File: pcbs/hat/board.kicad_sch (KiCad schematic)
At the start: 1 part, among them U17 NUCLEO-F401RE

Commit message: wip
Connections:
- net MEM_MISO: now also U17.CN7_2 (PC11); no longer U17.CN7_35 (PC2)
- net MEM_MOSI: now also U17.CN7_3 (PC12); no longer U17.CN7_37 (PC3)
- net MEM_SCK: now also U17.CN7_1 (PC10); no longer U17.CN10_25 (PB10)
- net SENSOR_13: now also U17.CN10_2 (PC8); no longer U17.CN10_4 (PC6)
- net SENSOR_23: now also U17.CN10_6 (PC5); no longer U17.CN10_19 (PC7)
- net SENSOR_33: no longer U17.CN10_2 (PC8)
- net SENSOR_43: no longer U17.CN10_1 (PC9)
- net SENSOR_53: no longer U17.CN10_16 (PB12)
- net SENSOR_63: no longer U17.CN10_30 (PB13)
- net SENSOR_73: no longer U17.CN10_28 (PB14)
- net SENSOR_83: no longer U17.CN10_26 (PB15)
- net SIGNAL_10: now also U17.CN10_12 (PA12); no longer U17.CN7_21 (PB7)
- net SIGNAL_11: now also U17.CN10_4 (PC6); no longer U17.CN10_13 (PA6)
- net SIGNAL_20: now also U17.CN10_16 (PB12); no longer U17.CN10_27 (PB4)
- net SIGNAL_21: now also U17.CN10_14 (PA11); no longer U17.CN10_15 (PA7)
- net SIGNAL_30: no longer U17.CN10_17 (PB6)
- net SIGNAL_31: no longer U17.CN7_34 (PB0)
- net SIGNAL_40: no longer U17.CN10_29 (PB5)
- net SIGNAL_41: no longer U17.CN10_24 (PB1)
- net SIGNAL_50: no longer U17.CN7_2 (PC11)
- net SIGNAL_51: no longer U17.CN10_23 (PA8)
- net SIGNAL_60: no longer U17.CN7_1 (PC10)
- net SIGNAL_61: no longer U17.CN10_21 (PA9)
- net SIGNAL_70: no longer U17.CN7_3 (PC12)
- net SIGNAL_71: no longer U17.CN10_33 (PA10)
- net SIGNAL_80: no longer U17.CN7_17 (PA15)
- net SIGNAL_81: no longer U17.CN10_14 (PA11)
- net ~{MEM_CE}: now also U17.CN7_4 (PD2); no longer U17.CN7_36 (PC1/PB9)

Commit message: wip
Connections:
- net SENSOR_13: now also U17.CN10_4 (PC6); no longer U17.CN10_2 (PC8)
- net SENSOR_33: now also U17.CN10_34 (PC4)
- net SENSOR_43: now also U17.CN10_29 (PB5)
- net SIGNAL_11: now also U17.CN10_2 (PC8); no longer U17.CN10_4 (PC6)
- net SIGNAL_21: now also U17.CN10_24 (PB1); no longer U17.CN10_14 (PA11)
- net SIGNAL_30: now also U17.CN10_30 (PB13)
- net SIGNAL_31: now also U17.CN10_33 (PA10)
- net SIGNAL_40: now also U17.CN10_28 (PB14)
- net SIGNAL_41: now also U17.CN10_27 (PB4)
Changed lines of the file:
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@@
+    (stroke (width 0) (type default) (color 0 0 0 0))
+  )
+  (bus_entry (at 170.18 57.15) (size -2.54 -2.54)
     (stroke (width 0) (type default) (color 0 0 0 0))
   )
@@
     (stroke (width 0) (type default) (color 0 0 0 0))
   )
-  (bus_entry (at 101.6 77.47) (size 2.54 -2.54)
+  (bus_entry (at 101.6 85.09) (size 2.54 -2.54)
     (stroke (width 0) (type default) (color 0 0 0 0))
   )
@@
     (stroke (width 0) (type default) (color 0 0 0 0))
   )
+  (bus_entry (at 101.6 95.25) (size 2.54 -2.54)
+    (stroke (width 0) (type default) (color 0 0 0 0))
+  )
+  (bus_entry (at 107.95 30.48) (size 2.54 -2.54)
+    (stroke (width 0) (type default) (color 0 0 0 0))
+  )
   (bus_entry (at -71.755 120.65) (size 2.54 -2.54)
     (stroke (width 0) (type default) (color 0 0 0 0))
@@
     (stroke (width 0) (type default) (color 0 0 0 0))
   )
+  (bus_entry (at 101.6 92.71) (size 2.54 -2.54)
+    (stroke (width 0) (type default) (color 0 0 0 0))
+  )
+  (bus_entry (at 101.6 74.93) (size 2.54 -2.54)
+    (stroke (width 0) (type default) (color 0 0 0 0))
+  )
   (bus_entry (at -68.58 90.17) (size 2.54 -2.54)
     (stroke (width 0) (type default) (color 0 0 0 0))
   )
+  (bus_entry (at 101.6 113.03) (size 2.54 -2.54)
+    (stroke (width 0) (type default) (color 0 0 0 0))
+  )
+  (bus_entry (at 101.6 110.49) (size 2.54 -2.54)
+    (stroke (width 0) (type default) (color 0 0 0 0))
+  )
   (bus_entry (at 101.6 107.95) (size 2.54 -2.54)
     (stroke (width 0) (type default) (color 0 0 0 0))
@@
     (stroke (width 0) (type default) (color 0 0 0 0))
   )
+  (bus_entry (at 163.83 30.48) (size -2.54 -2.54)
+    (stroke (width 0) (type default) (color 0 0 0 0))
+  )
   (bus_entry (at -68.58 107.95) (size 2.54 -2.54)
     (stroke (width 0) (type default) (color 0 0 0 0))
@@
     (stroke (width 0) (type default) (color 0 0 0 0))
   )
+  (wire (pts (xy 104.14 110.49) (xy 120.65 110.49))
+    (stroke (width 0) (type default) (color 0 0 0 0))
+  )
   (bus (pts (xy 98.425 19.05) (xy 170.18 19.05))
     (stroke (width 0) (type default) (color 0 0 0 0))
@@
     (stroke (width 0) (type default) (color 0 0 0 0))
   )
-  (bus (pts (xy 101.6 77.47) (xy 101.6 80.01))
-    (stroke (width 0) (type default) (color 0 0 0 0))
-  )
-  (bus (pts (xy 101.6 80.01) (xy 101.6 107.95))
-    (stroke (width 0) (type default) (color 0 0 0 0))
-  )
-  (bus (pts (xy 101.6 107.95) (xy 101.6 146.05))
+  (bus (pts (xy 101.6 80.01) (xy 101.6 85.09))
+    (stroke (width 0) (type default) (color 0 0 0 0))
+  )
+  (bus (pts (xy 101.6 107.95) (xy 101.6 110.49))
+    (stroke (width 0) (type default) (color 0 0 0 0))
+  )
+  (bus (pts (xy 101.6 110.49) (xy 101.6 113.03))
+    (stroke (width 0) (type default) (color 0 0 0 0))
+  )
+  (bus (pts (xy 101.6 74.93) (xy 101.6 80.01))
+    (stroke (width 0) (type default) (color 0 0 0 0))
+  )
+  (bus (pts (xy 170.18 57.15) (xy 170.18 59.69))
     (stroke (width 0) (type default) (color 0 0 0 0))
   )
@@
     (stroke (width 0) (type default) (color 0 0 0 0))
   )
-  (wire (pts (xy 104.14 74.93) (xy 120.65 74.93))
+  (bus (pts (xy 101.6 95.25) (xy 101.6 107.95))
+    (stroke (width 0) (type default) (color 0 0 0 0))
+  )
+  (wire (pts (xy 104.14 82.55) (xy 120.65 82.55))
     (stroke (width 0) (type default) (color 0 0 0 0))
   )
@@
     (stroke (width 0) (type default) (color 0 0 0 0))
   )
+  (wire (pts (xy 167.64 54.61) (xy 151.13 54.61))
+    (stroke (width 0) (type default) (color 0 0 0 0))
+  )
   (bus (pts (xy 31.75 19.05) (xy 98.425 19.05))
     (stroke (width 0) (type default) (color 0 0 0 0))
@@
     (stroke (width 0) (type default) (color 0 0 0 0))
   )
+  (wire (pts (xy 104.14 107.95) (xy 120.65 107.95))
+    (stroke (width 0) (type default) (color 0 0 0 0))
+  )
   (wire (pts (xy -28.575 110.49) (xy -12.065 110.49))
     (stroke (width 0) (type default) (color 0 0 0 0))
@@
     (stroke (width 0) (type default) (color 0 0 0 0))
   )
+  (wire (pts (xy 104.14 90.17) (xy 120.65 90.17))
+    (stroke (width 0) (type default) (color 0 0 0 0))
+  )
   (wire (pts (xy 104.14 77.47) (xy 120.65 77.47))
     (stroke (width 0) (type default) (color 0 0 0 0))
   )
+  (wire (pts (xy 110.49 27.94) (xy 127 27.94))
+    (stroke (width 0) (type default) (color 0 0 0 0))
+  )
   (wire (pts (xy -28.575 105.41) (xy -12.065 105.41))
     (stroke (width 0) (type default) (color 0 0 0 0))
@@
     (stroke (width 0) (type default) (color 0 0 0 0))
   )
+  (bus (pts (xy 101.6 113.03) (xy 101.6 146.05))
+    (stroke (width 0) (type default) (color 0 0 0 0))
+  )
   (wire (pts (xy 81.28 67.31) (xy 80.01 67.31))
     (stroke (width 0) (type default) (color 0 0 0 0))
@@
     (stroke (width 0) (type default) (color 0 0 0 0))
   )
+  (wire (pts (xy 161.29 27.94) (xy 144.78 27.94))
+    (stroke (width 0) (type default) (color 0 0 0 0))
+  )
   (wire (pts (xy 167.64 57.15) (xy 151.13 57.15))
     (stroke (width 0) (type default) (color 0 0 0 0))
   )
+  (wire (pts (xy 104.14 92.71) (xy 120.65 92.71))
+    (stroke (width 0) (type default) (color 0 0 0 0))
+  )
   (bus (pts (xy 101.6 146.05) (xy 261.62 146.05))
     (stroke (width 0) (type default) (color 0 0 0 0))
@@
     (stroke (width 0) (type default) (color 0 0 0 0))
   )
+  (bus (pts (xy 101.6 85.09) (xy 101.6 92.71))
+    (stroke (width 0) (type default) (color 0 0 0 0))
+  )
   (wire (pts (xy -66.04 87.63) (xy -49.53 87.63))
     (stroke (width 0) (type default) (color 0 0 0 0))
@@
     (stroke (width 0) (type default) (color 0 0 0 0))
   )
-  (bus (pts (xy 101.6 44.45) (xy 101.6 77.47))
+  (bus (pts (xy 101.6 44.45) (xy 101.6 74.93))
+    (stroke (width 0) (type default) (color 0 0 0 0))
+  )
+  (wire (pts (xy 104.14 72.39) (xy 120.65 72.39))
     (stroke (width 0) (type default) (color 0 0 0 0))
   )
@@
     (stroke (width 0) (type default) (color 0 0 0 0))
   )
-  (bus (pts (xy 170.18 19.05) (xy 170.18 59.69))
+  (bus (pts (xy 170.18 19.05) (xy 170.18 57.15))
+    (stroke (width 0) (type default) (color 0 0 0 0))
+  )
+  (bus (pts (xy 101.6 92.71) (xy 101.6 95.25))
     (stroke (width 0) (type default) (color 0 0 0 0))
   )
@@
     (effects (font (size 1.27 1.27)) (justify left bottom))
   )
-  (label "SIGNAL_21" (at 105.41 74.93 0)
+  (label "SIGNAL_21" (at 105.41 82.55 0)
     (effects (font (size 1.27 1.27)) (justify left bottom))
   )
@@
     (effects (font (size 1.27 1.27)) (justify left bottom))
   )
-  (label "SIGNAL_41" (at -65.405 95.25 0)
-    (effects (font (size 1.27 1.27)) (justify left bottom))
-  )
-  (label "SIGNAL_30" (at -65.405 107.95 0)
-    (effects (font (size 1.27 1.27)) (justify left bottom))
-  )
-  (label "SENSOR_33" (at -107.95 97.155 180)
+  (label "SIGNAL_41" (at 106.68 90.17 0)
+    (effects (font (size 1.27 1.27)) (justify left bottom))
+  )
+  (label "SIGNAL_30" (at 106.045 107.95 0)
+    (effects (font (size 1.27 1.27)) (justify left bottom))
+  )
+  (label "SENSOR_33" (at 165.1 54.61 180)
     (effects (font (size 1.27 1.27)) (justify right bottom))
   )
@@
     (effects (font (size 1.27 1.27)) (justify left bottom))
   )
-  (label "SIGNAL_40" (at -65.405 105.41 0)
-    (effects (font (size 1.27 1.27)) (justify left bottom))
-  )
-  (label "SIGNAL_11" (at 166.37 59.69 180)
-    (effects (font (size 1.27 1.27)) (justify right bottom))
-  )
-  (label "SENSOR_43" (at -107.95 99.695 180)
+  (label "SIGNAL_40" (at 107.95 110.49 0)
+    (effects (font (size 1.27 1.27)) (justify left bottom))
+  )
+  (label "SIGNAL_11" (at 163.83 64.77 180)
+    (effects (font (size 1.27 1.27)) (justify right bottom))
+  )
+  (label "SENSOR_43" (at 115.57 92.71 180)
     (effects (font (size 1.27 1.27)) (justify right bottom))
   )
@@
     (effects (font (size 1.27 1.27)) (justify left bottom))
   )
-  (label "SIGNAL_31" (at -27.94 87.63 0)
+  (label "SIGNAL_31" (at 106.68 72.39 0)
     (effects (font (size 1.27 1.27)) (justify left bottom))
   )
@@
     (effects (font (size 1.27 1.27)) (justify left bottom))
   )
-  (label "SENSOR_13" (at 167.005 64.77 180)
-    (effects (font (size 1.27 1.27)) (justify right bottom))
-  )
+  (label "SENSOR_13" (at 164.465 59.69 180)
+    (effects (font (size 1.27 1.27)) (justify right bottom))
+  )

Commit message: finish the pin assignment
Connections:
- net GND: now also U17.CN10_20 (GND_S2), U17.CN10_9 (GND_S2), U17.CN5_7 (GND_S6), U17.CN6_6 (GND), U17.CN6_7 (GND)
- net SENSOR_13: now also U17.CN10_2 (PC8); no longer U17.CN10_4 (PC6)
- net SENSOR_53: now also U17.CN10_25 (PB10)
- net SENSOR_63: now also U17.CN10_21 (PA9)
- net SENSOR_73: now also U17.CN7_36 (PC1/PB9)
- net SENSOR_83: now also U17.CN7_37 (PC3)
- net SIGNAL_11: now also U17.CN10_4 (PC6); no longer U17.CN10_2 (PC8)
- net SIGNAL_30: now also U17.CN10_33 (PA10); no longer U17.CN10_30 (PB13)
- net SIGNAL_31: now also U17.CN10_30 (PB13); no longer U17.CN10_33 (PA10)
- net SIGNAL_50: now also U17.CN10_23 (PA8)
- net SIGNAL_51: now also U17.CN10_22 (PB2)
- net SIGNAL_60: now also U17.CN10_19 (PC7)
- net SIGNAL_61: now also U17.CN10_17 (PB6)
- net SIGNAL_70: now also U17.CN7_38 (PC0/PB8)
- net SIGNAL_71: now also U17.CN7_30 (PA1)
- net SIGNAL_80: now also U17.CN7_35 (PC2)
- net SIGNAL_81: now also U17.CN7_28 (PA0)

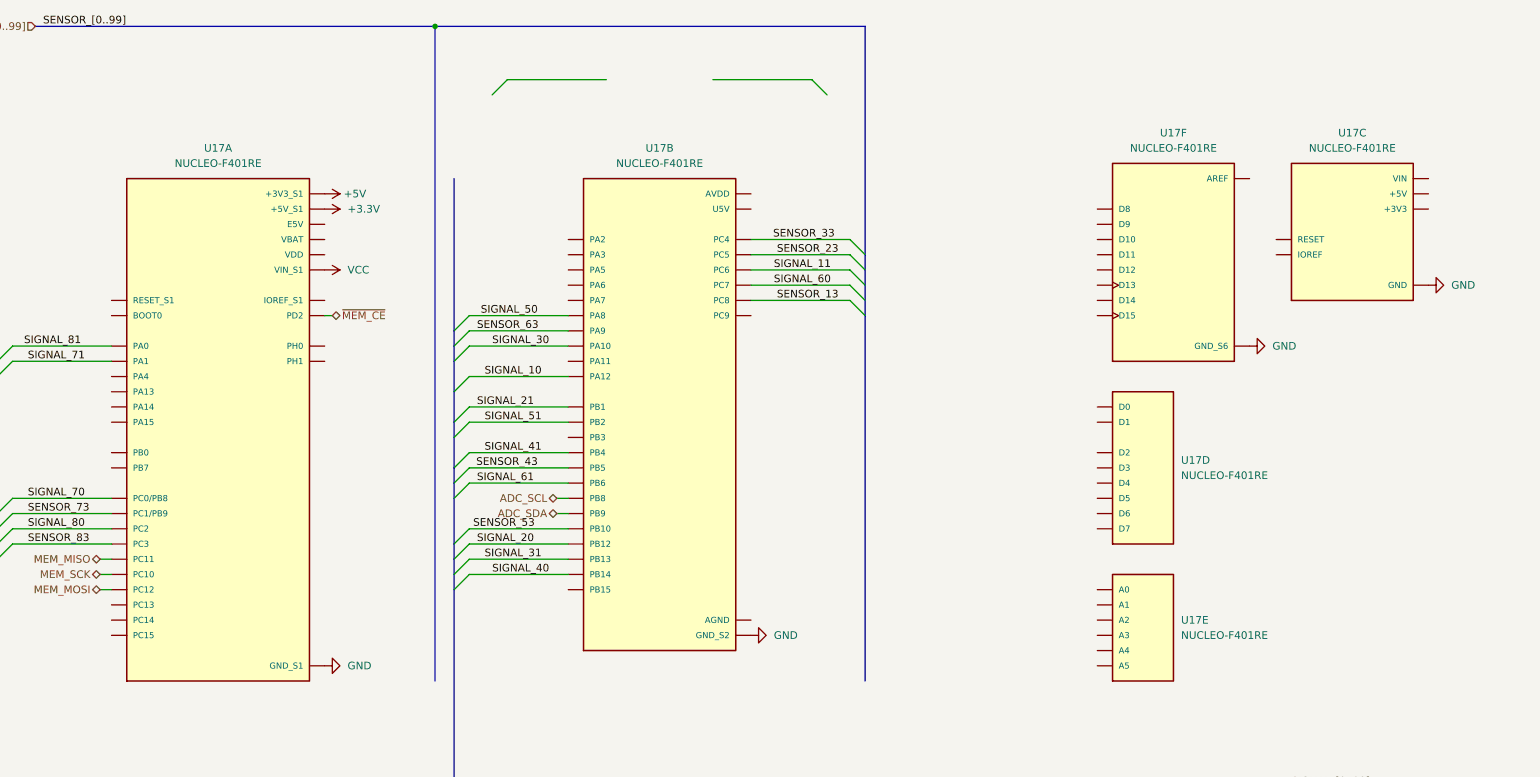
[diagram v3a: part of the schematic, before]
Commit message: reassign adc's
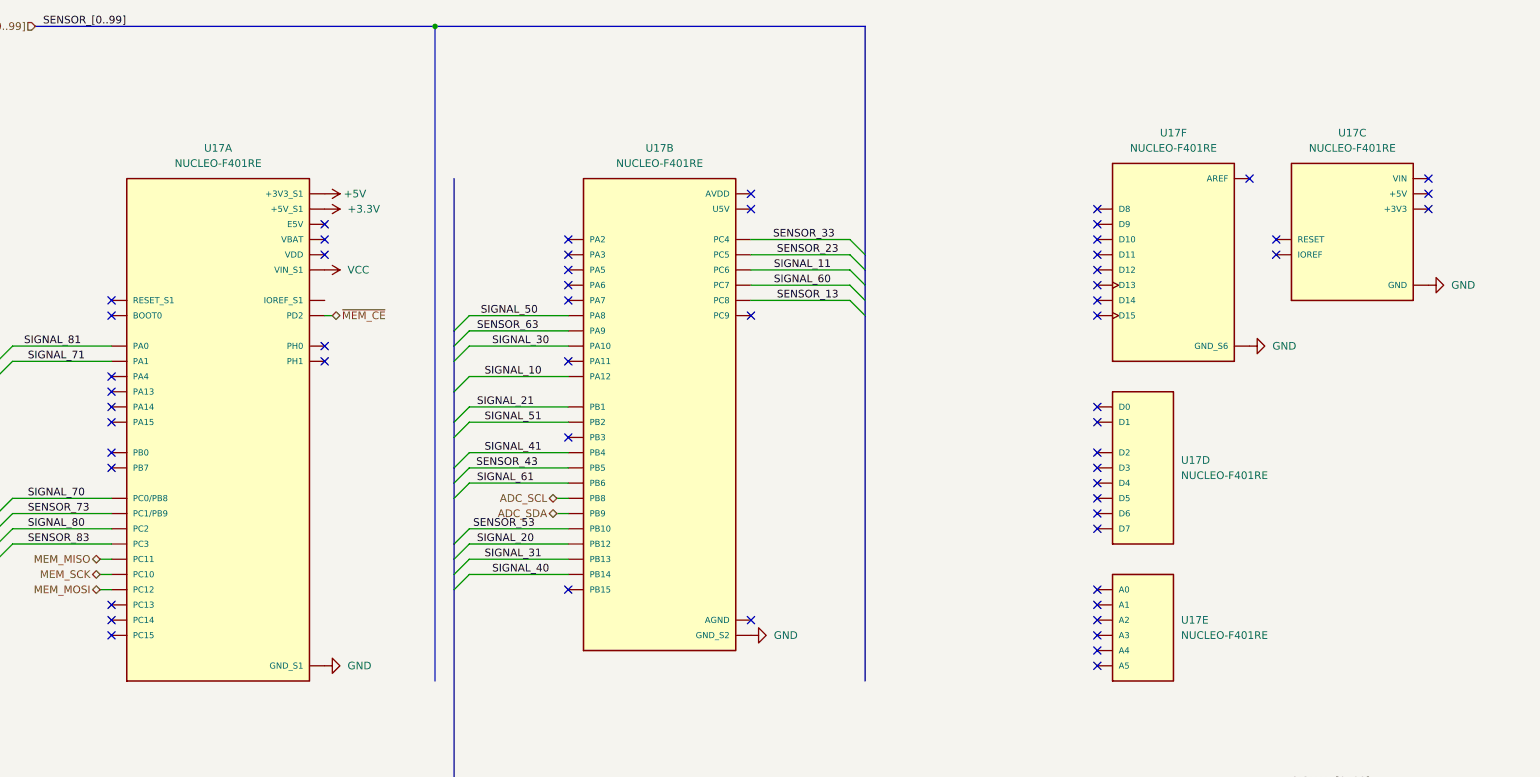
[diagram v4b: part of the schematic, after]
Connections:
- no-connect marks 0 -> 56
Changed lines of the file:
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@@
   (junction (at 101.6 146.05) (diameter 0) (color 0 0 0 0)
   )
+  (no_connect (at 208.915 54.61))
+  (no_connect (at 208.915 52.07))
+  (no_connect (at 208.915 90.17))
+  (no_connect (at 44.45 92.71))
+  (no_connect (at 151.13 46.99))
+  (no_connect (at 151.13 49.53))
+  (no_connect (at 151.13 67.31))
+  (no_connect (at 151.13 118.11))
+  (no_connect (at 208.915 125.73))
+  (no_connect (at 234.315 44.45))
+  (no_connect (at 264.16 46.99))
+  (no_connect (at 208.915 62.23))
+  (no_connect (at 208.915 85.09))
+  (no_connect (at 208.915 82.55))
+  (no_connect (at 208.915 113.03))
+  (no_connect (at 44.45 118.11))
+  (no_connect (at 264.16 49.53))
+  (no_connect (at 208.915 95.25))
+  (no_connect (at 208.915 49.53))
+  (no_connect (at 208.915 59.69))
+  (no_connect (at 208.915 102.87))
+  (no_connect (at 208.915 64.77))
+  (no_connect (at 44.45 120.65))
+  (no_connect (at 44.45 115.57))
+  (no_connect (at 208.915 57.15))
+  (no_connect (at 208.915 100.33))
+  (no_connect (at 120.65 74.93))
+  (no_connect (at 120.65 113.03))
+  (no_connect (at 120.65 87.63))
+  (no_connect (at 120.65 64.77))
+  (no_connect (at 120.65 62.23))
+  (no_connect (at 120.65 59.69))
+  (no_connect (at 120.65 57.15))
+  (no_connect (at 120.65 54.61))
+  (no_connect (at 80.01 72.39))
+  (no_connect (at 80.01 74.93))
+  (no_connect (at 80.01 57.15))
+  (no_connect (at 80.01 54.61))
+  (no_connect (at 80.01 52.07))
+  (no_connect (at 44.45 80.01))
+  (no_connect (at 44.45 90.17))
+  (no_connect (at 44.45 82.55))
+  (no_connect (at 208.915 67.31))
+  (no_connect (at 44.45 77.47))
+  (no_connect (at 44.45 85.09))
+  (no_connect (at 44.45 67.31))
+  (no_connect (at 44.45 64.77))
+  (no_connect (at 208.915 123.19))
+  (no_connect (at 208.915 120.65))
+  (no_connect (at 208.915 97.79))
+  (no_connect (at 208.915 92.71))
+  (no_connect (at 208.915 115.57))
+  (no_connect (at 208.915 118.11))
+  (no_connect (at 238.76 57.15))
+  (no_connect (at 264.16 44.45))
+  (no_connect (at 238.76 54.61))
   (bus_entry (at 101.6 97.79) (size 2.54 -2.54)
     (stroke (width 0) (type default) (color 0 0 0 0))
@@
     (stroke (width 0) (type default) (color 0 0 0 0))
   )
-  (bus_entry (at 107.95 30.48) (size 2.54 -2.54)
-    (stroke (width 0) (type default) (color 0 0 0 0))
-  )
   (bus_entry (at 101.6 72.39) (size 2.54 -2.54)
     (stroke (width 0) (type default) (color 0 0 0 0))
@@
     (stroke (width 0) (type default) (color 0 0 0 0))
   )
-  (bus_entry (at 163.83 30.48) (size -2.54 -2.54)
-    (stroke (width 0) (type default) (color 0 0 0 0))
-  )
   (bus_entry (at 170.18 62.23) (size -2.54 -2.54)
     (stroke (width 0) (type default) (color 0 0 0 0))
@@
     (stroke (width 0) (type default) (color 0 0 0 0))
   )
-  (wire (pts (xy 110.49 27.94) (xy 127 27.94))
-    (stroke (width 0) (type default) (color 0 0 0 0))
-  )
   (wire (pts (xy 104.14 95.25) (xy 120.65 95.25))
     (stroke (width 0) (type default) (color 0 0 0 0))
@@
     (stroke (width 0) (type default) (color 0 0 0 0))
   )
-  (wire (pts (xy 161.29 27.94) (xy 144.78 27.94))
-    (stroke (width 0) (type default) (color 0 0 0 0))
-  )

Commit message: pcb layout progress
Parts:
- U17: footprint STS_Boards:ST_Morpho_Connector_64_MountingHoles -> STS_Boards:ST_Morpho_Connector_64
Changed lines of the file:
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@@
   (no_connect (at 151.13 67.31))
   (no_connect (at 151.13 118.11))
+  (no_connect (at 234.315 44.45))
   (no_connect (at 208.915 125.73))
-  (no_connect (at 234.315 44.45))
   (no_connect (at 264.16 46.99))
   (no_connect (at 208.915 62.23))
@@
   (no_connect (at 44.45 77.47))
   (no_connect (at 44.45 85.09))
+  (no_connect (at 44.45 64.77))
   (no_connect (at 44.45 67.31))
-  (no_connect (at 44.45 64.77))
   (no_connect (at 208.915 123.19))
   (no_connect (at 208.915 120.65))
@@
       (effects (font (size 1.27 1.27)) (justify left))
     )
-    (property "Footprint" "STS_Boards:ST_Morpho_Connector_64_MountingHoles" (id 2) (at 211.455 92.71 0)
+    (property "Footprint" "STS_Boards:ST_Morpho_Connector_64" (id 2) (at 211.455 92.71 0)
       (effects (font (size 1.27 1.27)) (justify left bottom) hide)
     )
@@
     (property "Reference" "U17" (id 0) (at 251.46 36.83 0))
     (property "Value" "NUCLEO-F401RE" (id 1) (at 251.46 39.37 0))
-    (property "Footprint" "STS_Boards:ST_Morpho_Connector_64_MountingHoles" (id 2) (at 246.38 52.07 0)
+    (property "Footprint" "STS_Boards:ST_Morpho_Connector_64" (id 2) (at 246.38 52.07 0)
       (effects (font (size 1.27 1.27)) (justify left bottom) hide)
     )
@@
     (property "Reference" "U17" (id 0) (at 62.23 39.37 0))
     (property "Value" "NUCLEO-F401RE" (id 1) (at 62.23 41.91 0))
-    (property "Footprint" "STS_Boards:ST_Morpho_Connector_64_MountingHoles" (id 2) (at 57.15 85.09 0)
+    (property "Footprint" "STS_Boards:ST_Morpho_Connector_64" (id 2) (at 57.15 85.09 0)
       (effects (font (size 1.27 1.27)) (justify left bottom) hide)
     )
@@
       (effects (font (size 1.27 1.27)) (justify left))
     )
-    (property "Footprint" "STS_Boards:ST_Morpho_Connector_64_MountingHoles" (id 2) (at 211.455 118.11 0)
+    (property "Footprint" "STS_Boards:ST_Morpho_Connector_64" (id 2) (at 211.455 118.11 0)
       (effects (font (size 1.27 1.27)) (justify left bottom) hide)
     )
@@
     (property "Reference" "U17" (id 0) (at 135.89 39.37 0))
     (property "Value" "NUCLEO-F401RE" (id 1) (at 135.89 41.91 0))
-    (property "Footprint" "STS_Boards:ST_Morpho_Connector_64_MountingHoles" (id 2) (at 130.81 82.55 0)
+    (property "Footprint" "STS_Boards:ST_Morpho_Connector_64" (id 2) (at 130.81 82.55 0)
       (effects (font (size 1.27 1.27)) (justify left bottom) hide)
     )
@@
     (property "Reference" "U17" (id 0) (at 221.615 36.83 0))
     (property "Value" "NUCLEO-F401RE" (id 1) (at 221.615 39.37 0))
-    (property "Footprint" "STS_Boards:ST_Morpho_Connector_64_MountingHoles" (id 2) (at 216.535 57.15 0)
-      (effects (font (size 1.27 1.27)) (justify left bottom) hide)
-    )
+    (property "Footprint" "STS_Boards:ST_Morpho_Connector_64" (id 2) (at 216.535 57.15 0)
+      (effects (font (size 1.27 1.27)) (justify left bottom) hide)
+    )
